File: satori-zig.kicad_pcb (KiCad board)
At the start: 2 copper layers, 70 x 25 mm, 8 parts

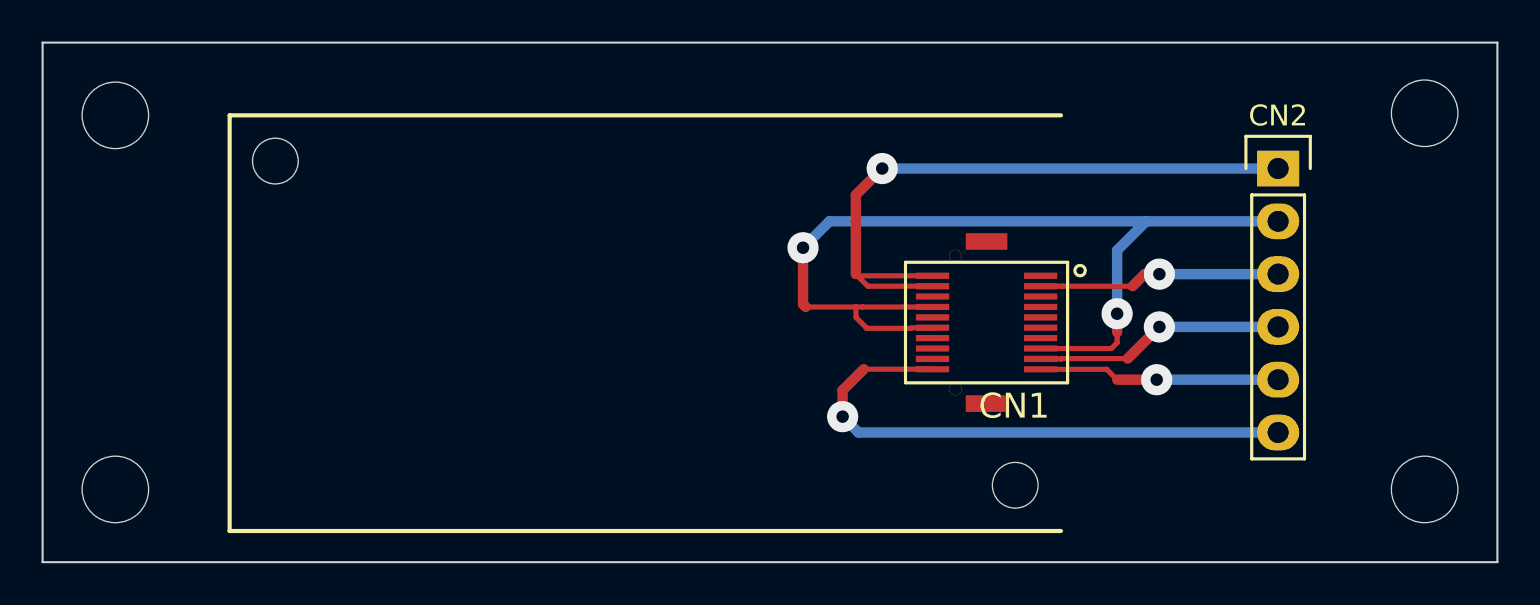
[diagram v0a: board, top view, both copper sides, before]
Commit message: ベタグランド化
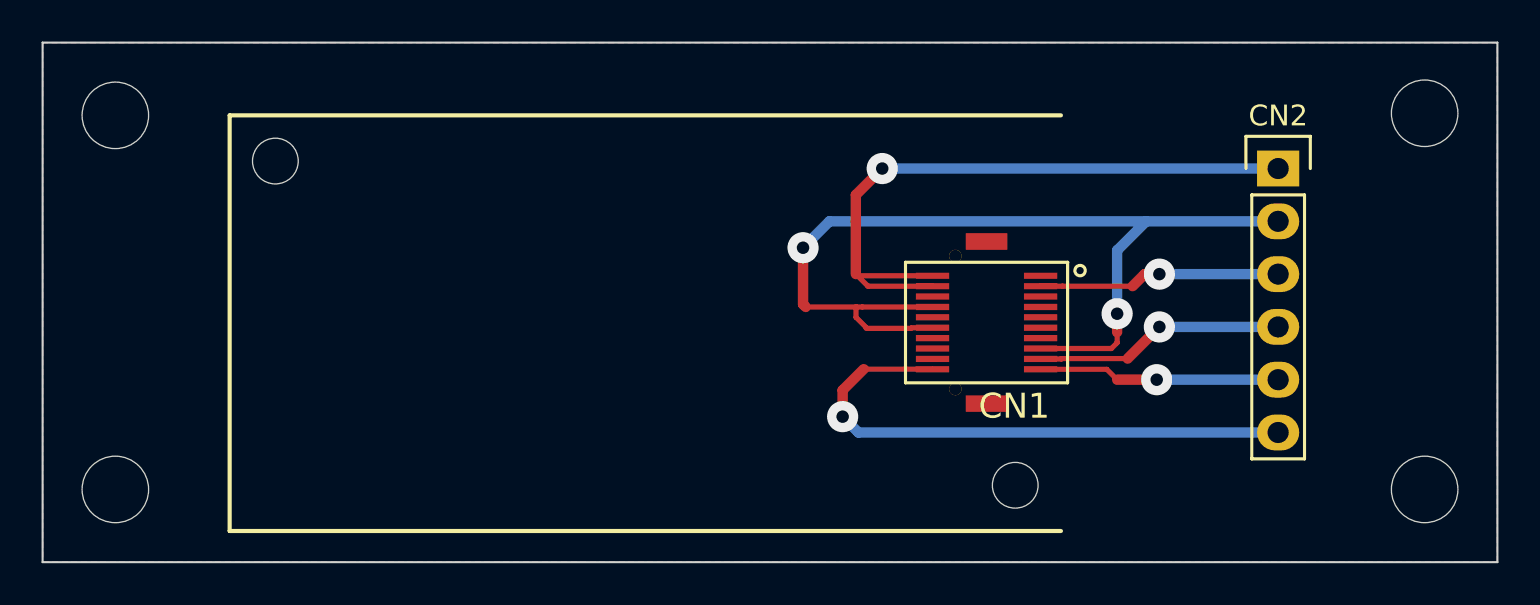
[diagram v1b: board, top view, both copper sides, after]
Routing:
- added copper zone on B.Cu, net GND
- added copper zone on F.Cu, net GND
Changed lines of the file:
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@@
+    )
+  )
+  (zone (net 6) (net_name GND) (layer B.Cu) (hatch edge 0.508)
+    (connect_pads (clearance 0.508))
+    (min_thickness 0.254)
+    (fill yes (arc_segments 16) (thermal_gap 0.508) (thermal_bridge_width 0.508))
+    (polygon
+      (pts
+        (xy 182 118) (xy 182 93) (xy 112 93) (xy 112 118)
+      )
+    )
+  )
+  (zone (net 6) (net_name GND) (layer F.Cu) (hatch edge 0.508)
+    (connect_pads (clearance 0.508))
+    (min_thickness 0.254)
+    (fill yes (arc_segments 16) (thermal_gap 0.508) (thermal_bridge_width 0.508))
+    (polygon
+      (pts
+        (xy 182 118) (xy 182 93) (xy 112 93) (xy 112 118)
+      )
     )
   )
